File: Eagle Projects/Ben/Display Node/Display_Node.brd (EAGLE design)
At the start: 100 x 100 mm, 43 parts, among them Q1 16MHz, Q3 16MHz, Q4 16MHz, Q5 16MHz, Q6 2N7002, Q7 2N7002, U1 ATMEGA328P_TQFP, U2 MCP2551, X1 5566-6, X2 5566-6

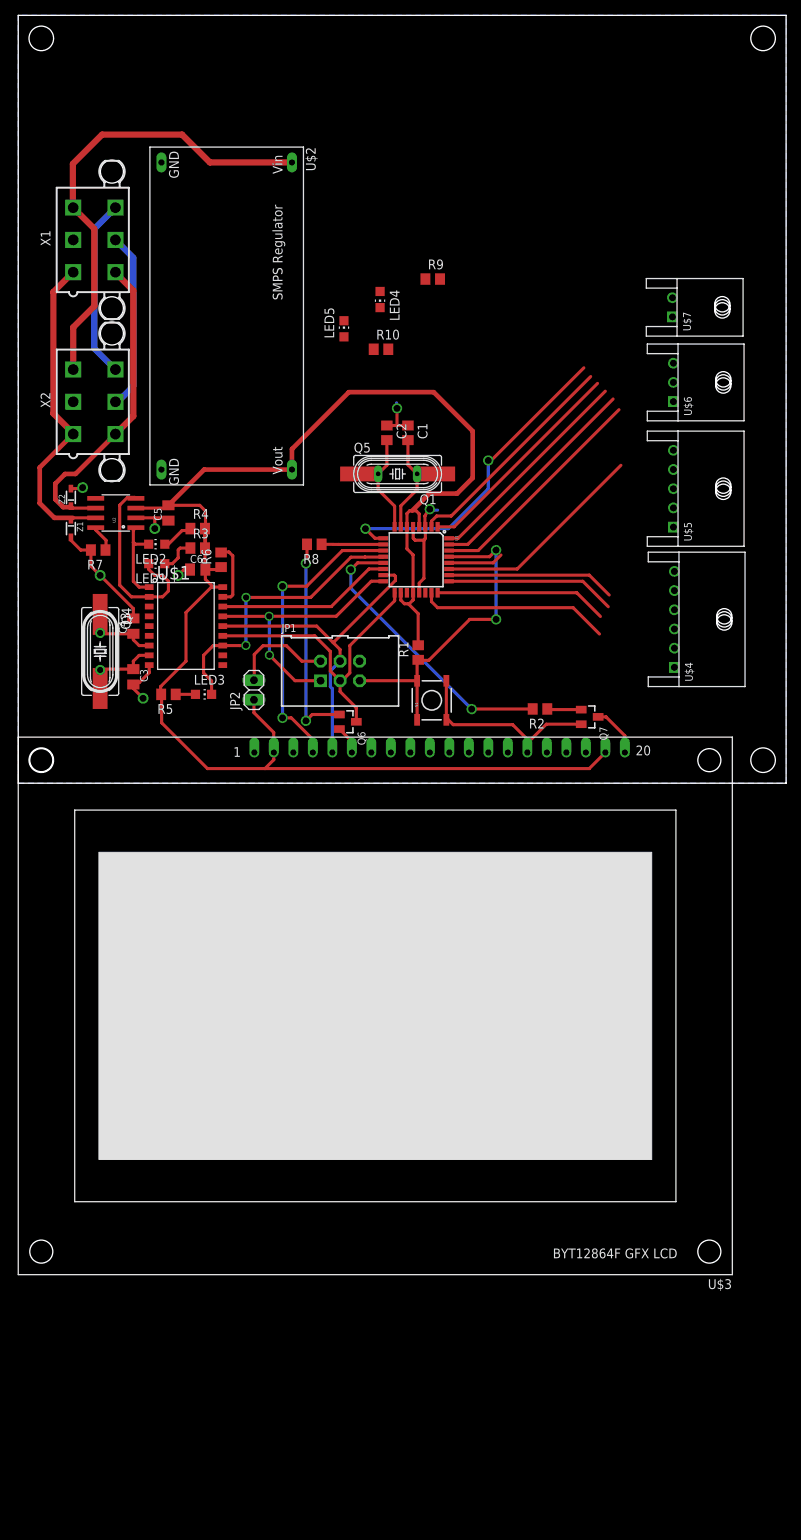
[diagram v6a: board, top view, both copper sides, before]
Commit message: Display node nearly done
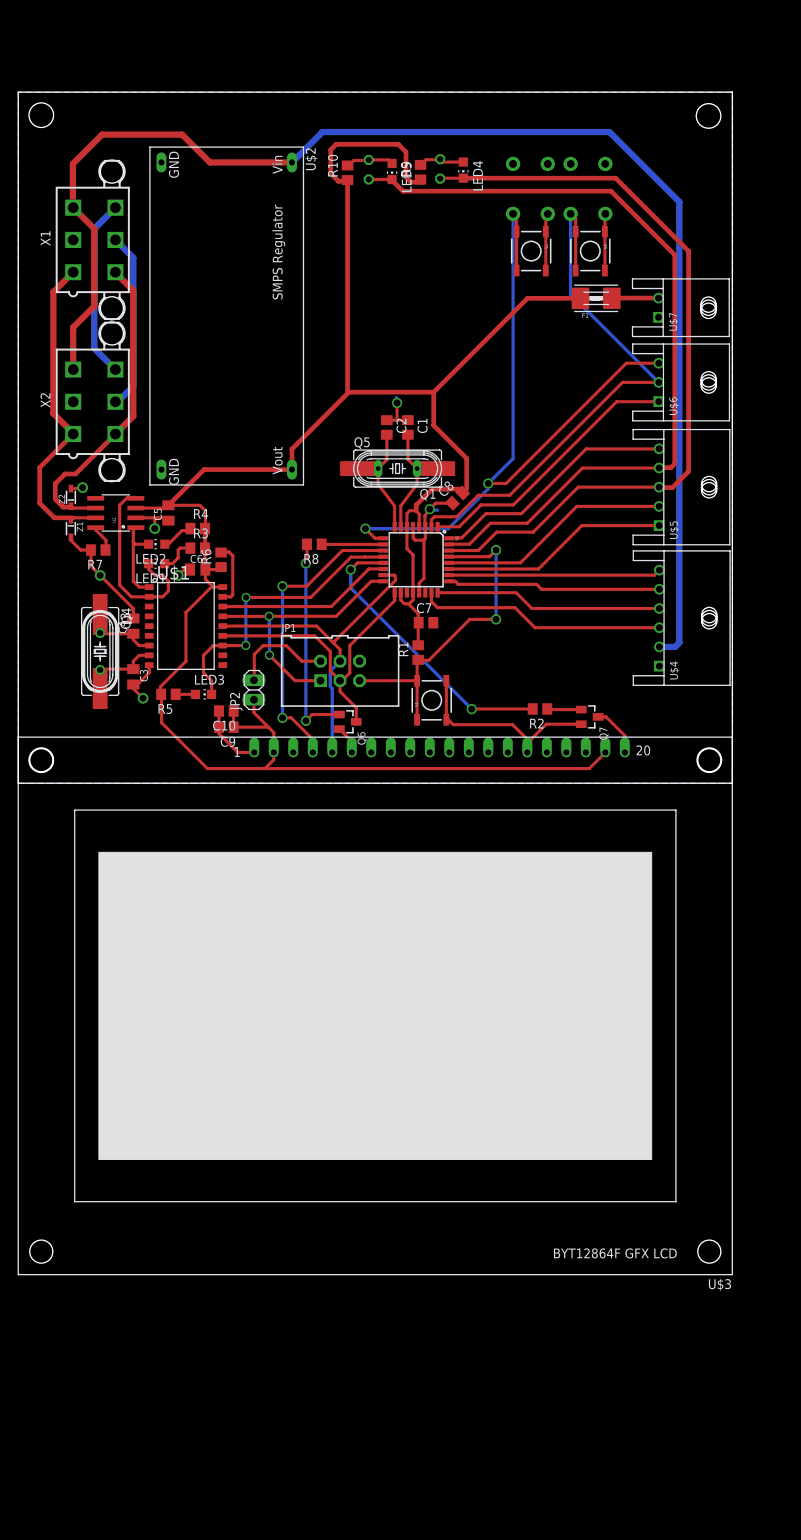
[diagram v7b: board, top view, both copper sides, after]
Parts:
- added C10: 10uF, resistor:C0805
- added C7, C8, C9: 100nF, resistor:C0805
- added F1: (no value), adafruit:1812
- added LED6, LED7: (no value), led:LED5MM
- added S2, S3: SWITCH-MOMENTARY-2PTH, SparkFun:TACTILE-PTH
- added S4: BTN3, SparkFun:TACTILE_SWITCH_SMD
- added S5: BTN4, SparkFun:TACTILE_SWITCH_SMD
- moved R10 23.4 mm to (42.9, 79.5), turned to 90 degrees
- moved LED5 21.4 mm to (48.7, 79.7), turned to 180 degrees
- moved LED4 20.0 mm to (58.0, 79.8)
- moved R9 14.0 mm to (52.4, 79.6), turned to 90 degrees
- moved U$4 1.95 mm to (90.0, 21.5)
- moved U$6 1.90 mm to (89.9, 52.2)
- moved U$5 1.86 mm to (90.0, 38.6)
- moved U$7 1.80 mm to (89.9, 61.9)
- moved C1 0.70 mm to (50.7, 46.3)
- moved C2 0.70 mm to (48.0, 46.3)
- moved Q1 0.70 mm to (49.4, 41.0)
- moved Q5 0.70 mm to (49.4, 41.0)
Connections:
- removed net N$23: U$4.P$2
- removed net N$24: U$4.P$1
- new net N$17: F1.2, U$7.P$2
- net +12V: now also U$4.P$2
- net +5V: now also C10.1, C7.2, C8.2, C9.1, F1.1
- net A0: now also U$5.P$1
- net A1: now also U$5.P$2
- net BTN1: now also U$5.P$5
- net BTN2: now also U$6.P$1
- net BTN3: now also S2.3, S4.3, S4.4, U$6.P$2
- net BTN4: now also S3.3, S5.3, S5.4, U$6.P$3
- net CRUISE1: now also U$4.P$3; no longer U$4.P$6
- net CRUISE2: now also U$4.P$4; no longer U$4.P$5
- net CRUISE3: now also U$4.P$5; no longer U$4.P$4
- net CRUISE4: now also U$4.P$6; no longer U$4.P$3
- net GND: now also C10.2, C7.1, C8.1, C9.2, S2.1, S3.1, S4.1, S4.2, S5.1, S5.2, U$4.P$1, U$7.P$1
- net LED1: now also LED7.K, U$5.P$3
- net LED2: now also LED6.K, U$5.P$4
- net N$13: now also LED7.A
- net N$16: now also LED6.A
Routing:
- net +12V: track 60.7 -> 176.8 mm
- net +5V: track 209.4 -> 290.5 mm
- net LED2: track 29.2 -> 104.9 mm
- net LED1: track 29.7 -> 100.4 mm
- net BTN4: track 42.1 -> 94.4 mm
- net BTN3: track 29.3 -> 72.3 mm
- net GND: track 77.3 -> 104.0 mm
- net A1: track 7.18 -> 30.4 mm
- net CRUISE1: track 24.8 -> 32.2 mm
- net CRUISE2: track 22.5 -> 29.7 mm
- net BTN2: track 28.6 -> 35.6 mm
- net N$16: track 0.00 -> 6.28 mm
- net N$17: track 0.00 -> 6.10 mm
- net N$13: track 0.00 -> 6.04 mm
- net CRUISE4: track 21.9 -> 27.7 mm
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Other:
- board size 100 x 100 mm -> 93 x 90 mm

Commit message: Working On Protection
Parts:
- added R11, R12, R13, R14: 470E, resistor:R0805
- added U$10, U$11, U$8, U$9: DRTR5V0U1SO, RobThePyro:SOT23
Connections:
- new net N$18: R11.1, U$6.P$3
- new net N$19: R12.1, U$6.P$2
- new net N$20: R13.1, U$6.P$1
- new net N$21: R14.1, U$5.P$5
- net +5V: now also U$10.2, U$11.2, U$8.2, U$9.2
- net BTN1: now also R14.2, U$11.1; no longer U$5.P$5
- net BTN2: now also R13.2, U$10.1; no longer U$6.P$1
- net BTN3: now also R12.2, U$9.1; no longer U$6.P$2
- net BTN4: now also R11.2, U$8.1; no longer U$6.P$3
- net GND: now also U$10.3, U$11.3, U$8.3, U$9.3
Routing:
- net LED2: track 104.9 -> 76.1 mm
- net LED1: track 100.4 -> 73.4 mm
- net +5V: track 290.5 -> 313.7 mm, vias 0 -> 4
- net A1: track 30.4 -> 9.30 mm
- net A0: track 29.7 -> 11.6 mm
- net BTN3: track 72.3 -> 54.5 mm
- net GND: track 104.0 -> 111.6 mm, vias 7 -> 11
- net BTN1: track 32.2 -> 26.4 mm
- net N$20: track 0.00 -> 4.57 mm
- net N$19: track 0.00 -> 4.57 mm
- net N$21: track 0.00 -> 4.55 mm
- net N$18: track 0.00 -> 4.55 mm
- net BTN2: track 35.6 -> 31.7 mm
